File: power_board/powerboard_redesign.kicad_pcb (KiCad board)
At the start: 2 copper layers, 80 x 53 mm, 17 parts, among them J1 282834-2, J2 282834-2, J3 282834-2, J4 282834-2, U1 PDQ30-Q24-D12-D

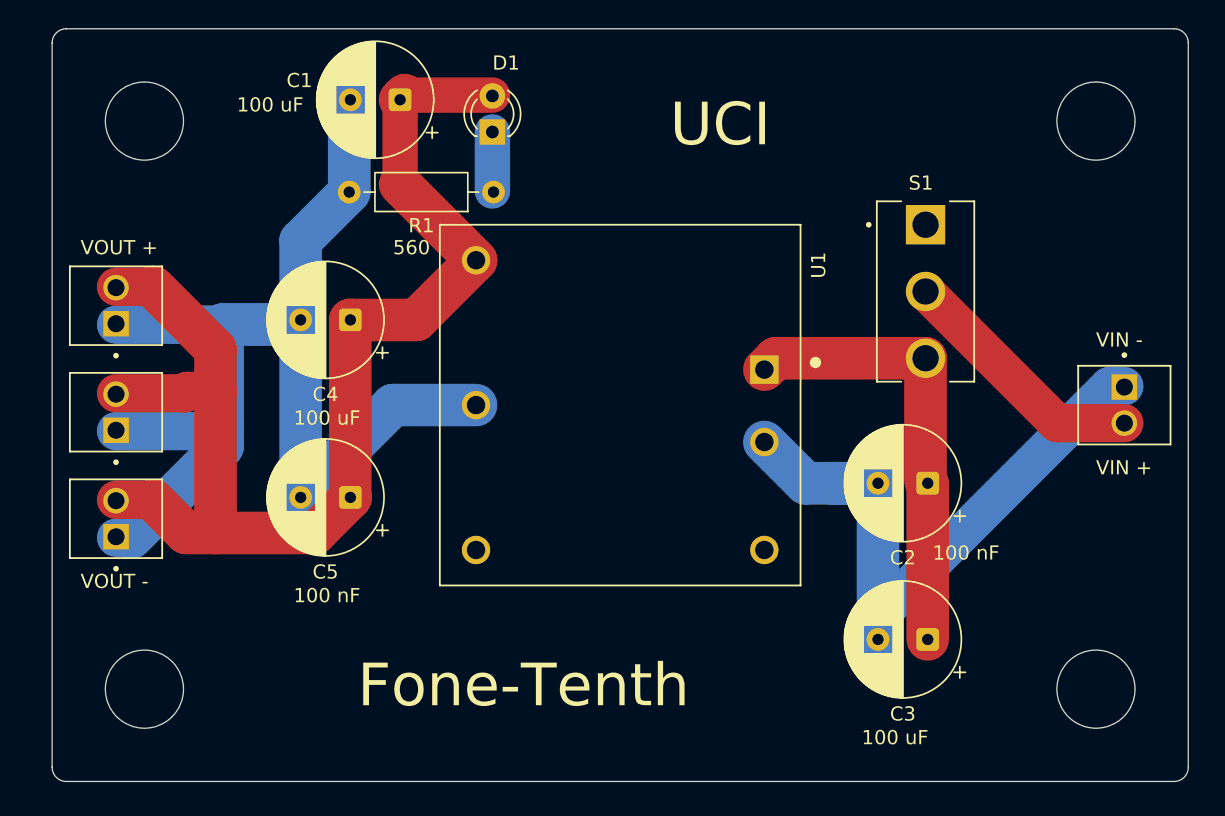
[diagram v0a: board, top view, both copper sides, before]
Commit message: Updated PCB with new connectors
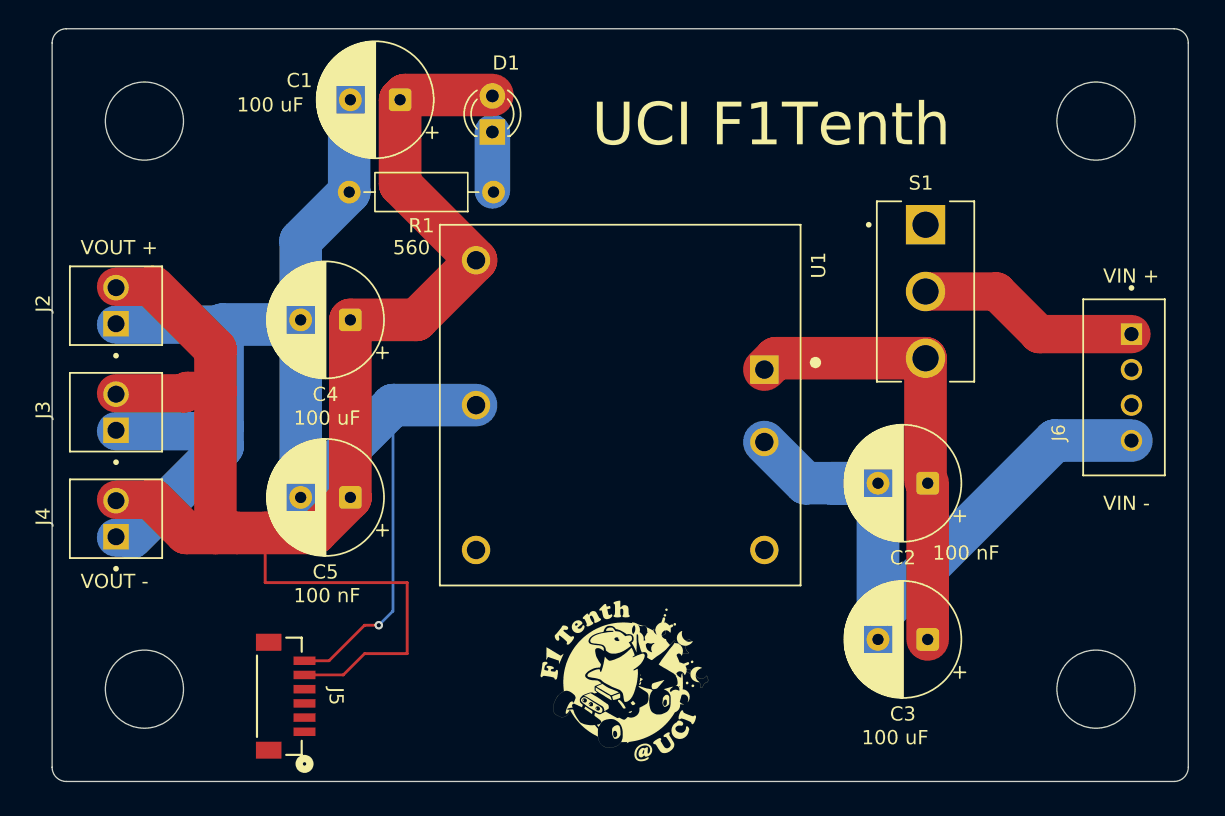
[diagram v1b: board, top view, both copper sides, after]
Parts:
- removed J1: 282834-2, Library3:TE_282834-2
- added J5: BM06B-SRSS-TBLFSN, F1TenthPowerBoard:CONN_BM06B-SRSS-TB_JST, F.Cu at (121.0, 120.0)
- added J6: B4B-XH-A, F1TenthPowerBoard:JST_B4B-XH-A, F.Cu at (180.5, 98.2)
- added Ref: LOGO, F1TenthPowerBoard:F1TenthUCILogo, F.Cu at (146.0, 119.0)
- J2, J3, J4: footprint Library3:TE_282834-2 -> F1TenthPowerBoard:TE_282834-2
- S1: footprint Library2:SW_100SP1T1B4M2QE -> F1TenthPowerBoard:SW_100SP1T1B4M2QE
- U1: footprint Library:CONV_PDQ30-Q24-D12-D -> F1TenthPowerBoard:CONV_PDQ30-Q24-D12-D
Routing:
- net Net-(D1-A): track 90.6 -> 116.9 mm
- net Net-(U1-COMMON): track 84.2 -> 106.4 mm, vias 0 -> 1
- net Net-(J6-Pad1): track 17.8 -> 15.7 mm
- net Net-(U1--VIN): track 49.2 -> 48.1 mm
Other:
- board text added: "For more information, visit: https://github.com/uci-f1tenth/Power-board Last Updated: Apr 1, 2026"
- board text added: "UCI F1Tenth"
- board text removed: "Fone-Tenth"
- board text removed: "For more information, visit: https://github.com/uci-f1tenth/Power-board Last Updated: Feb 12, 2026"
- board text removed: "UCI"

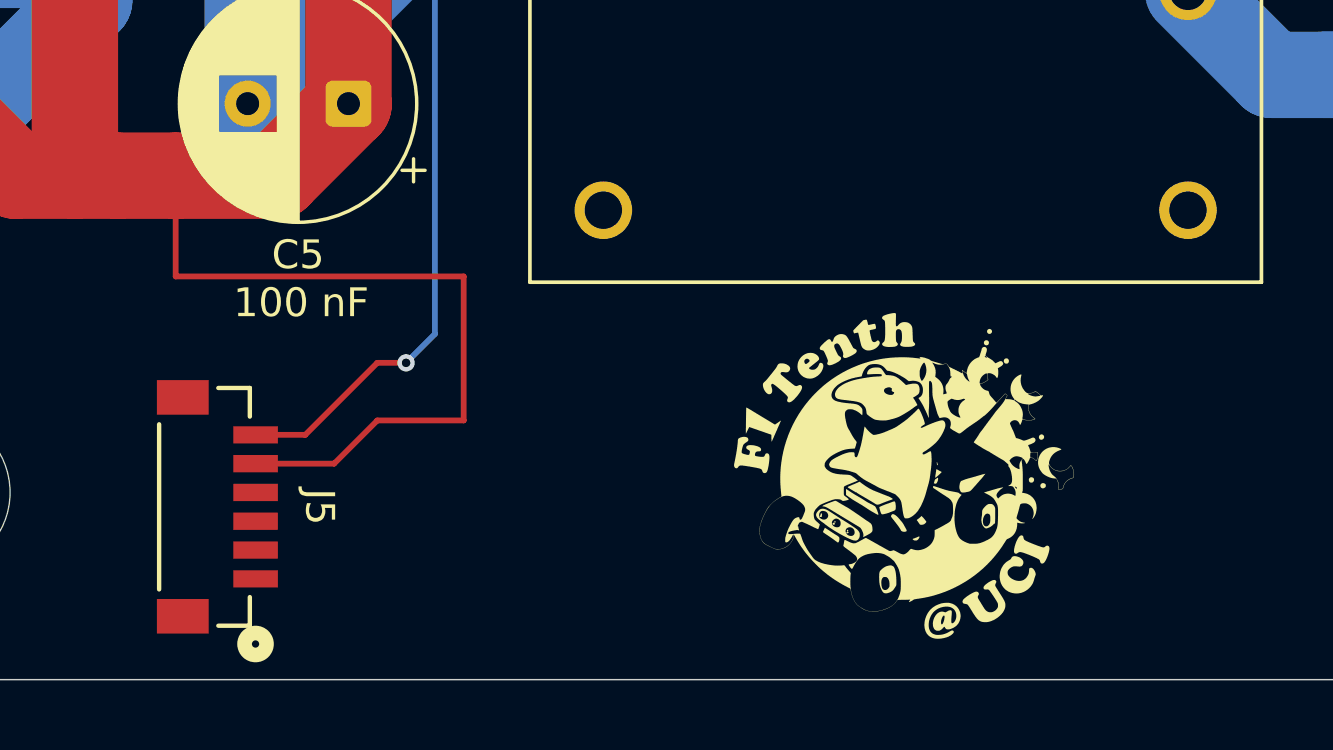
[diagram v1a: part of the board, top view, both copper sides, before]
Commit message: Updated schematic and PCB for V3
Added 4-pin connector for LiDAR connector
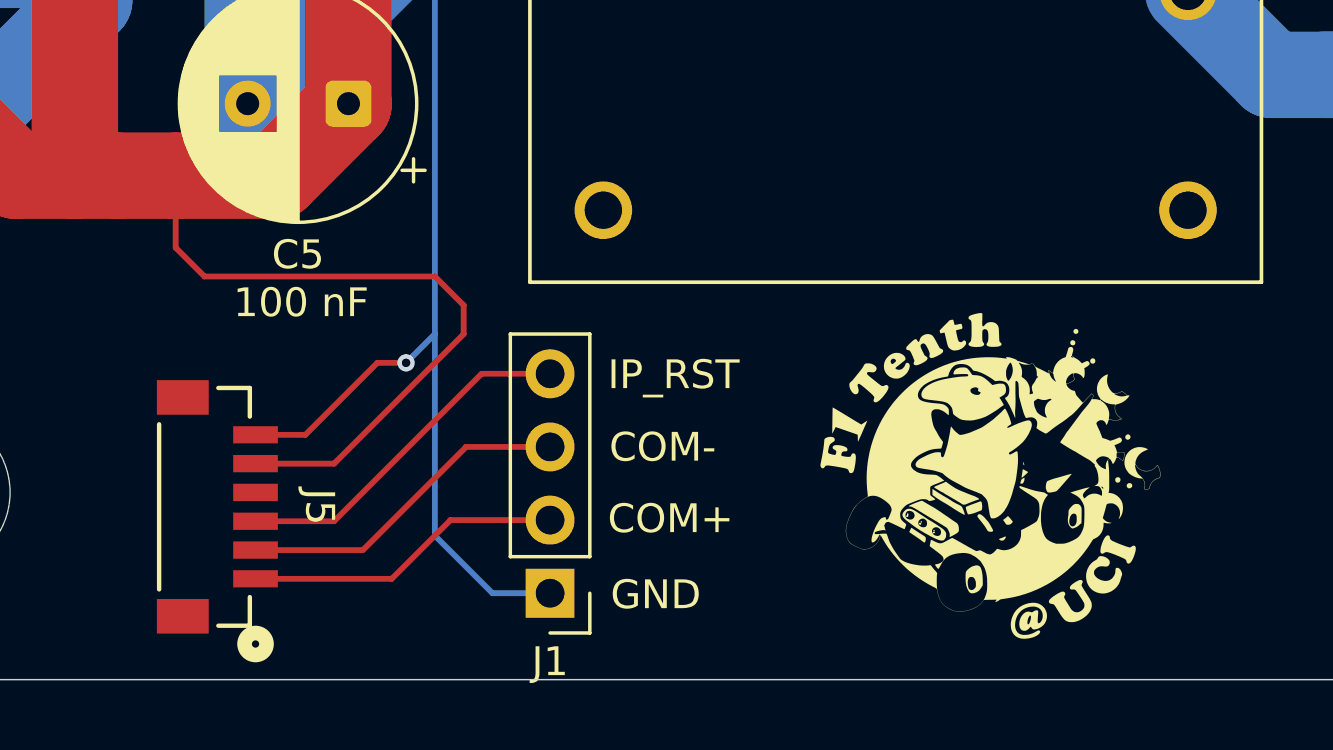
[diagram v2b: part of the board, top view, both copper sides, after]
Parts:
- added J1: Conn_01x04_Pin, Connector_PinHeader_2.54mm:PinHeader_1x04_P2.54mm_Vertical, F.Cu at (133.0, 123.0)
- moved Ref 3.00 mm to (149.0, 119.0)
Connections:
- J5 pad 1: unconnected-(J5-Pad1) -> Net-(J1-Pin_2)
- J5 pad 2: unconnected-(J5-Pad2) -> Net-(J1-Pin_3)
- J5 pad 3: unconnected-(J5-Pad3) -> Net-(J1-Pin_4)
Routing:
- net Net-(J1-Pin_4): track 0.00 -> 12.3 mm
- net Net-(J1-Pin_1): track 106.4 -> 118.2 mm
- net Net-(J1-Pin_3): track 0.00 -> 11.7 mm
- net Net-(J1-Pin_2): track 0.00 -> 11.1 mm
- net Net-(D1-A): track 116.9 -> 114.0 mm
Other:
- board text added: "COM+"
- board text added: "COM-"
- board text added: "GND"
- board text added: "IP_RST"

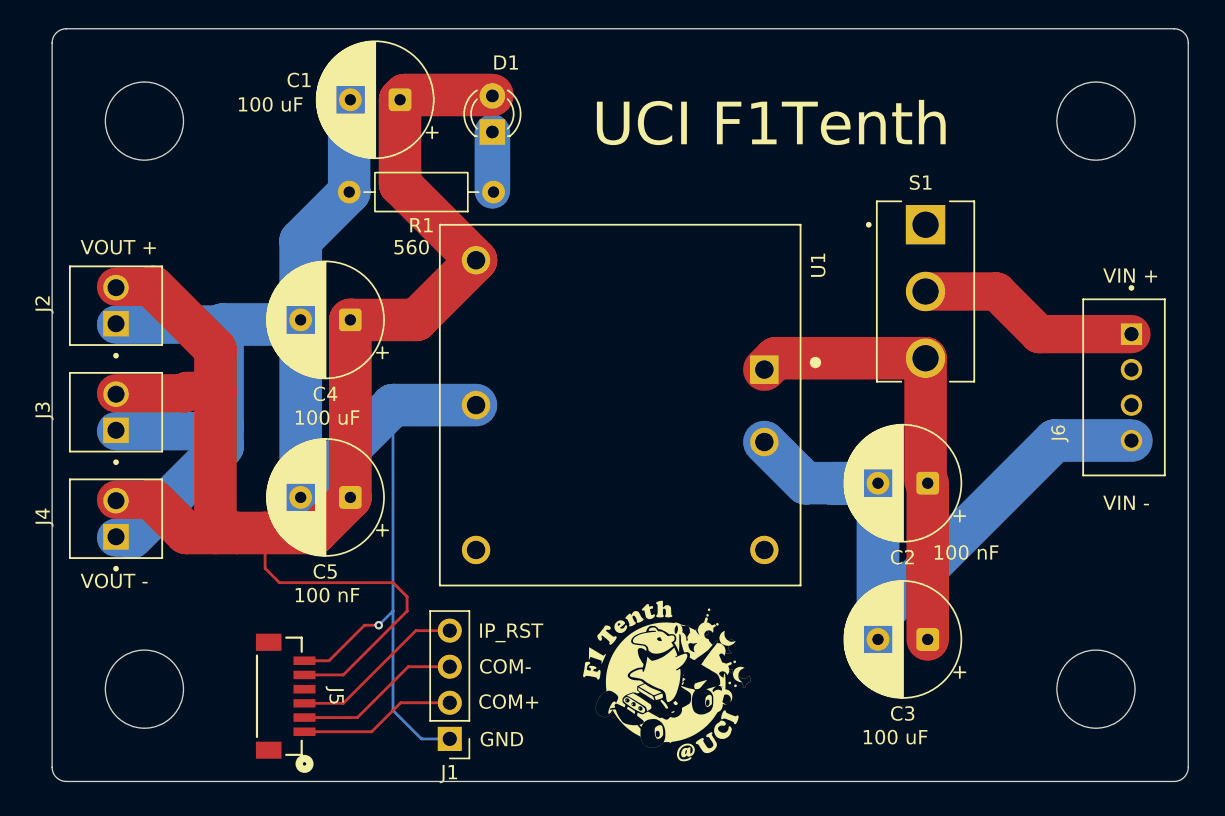
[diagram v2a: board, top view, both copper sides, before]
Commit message: Updated PCB with S12 Buck Converter + extra screw terminal block on Battery side
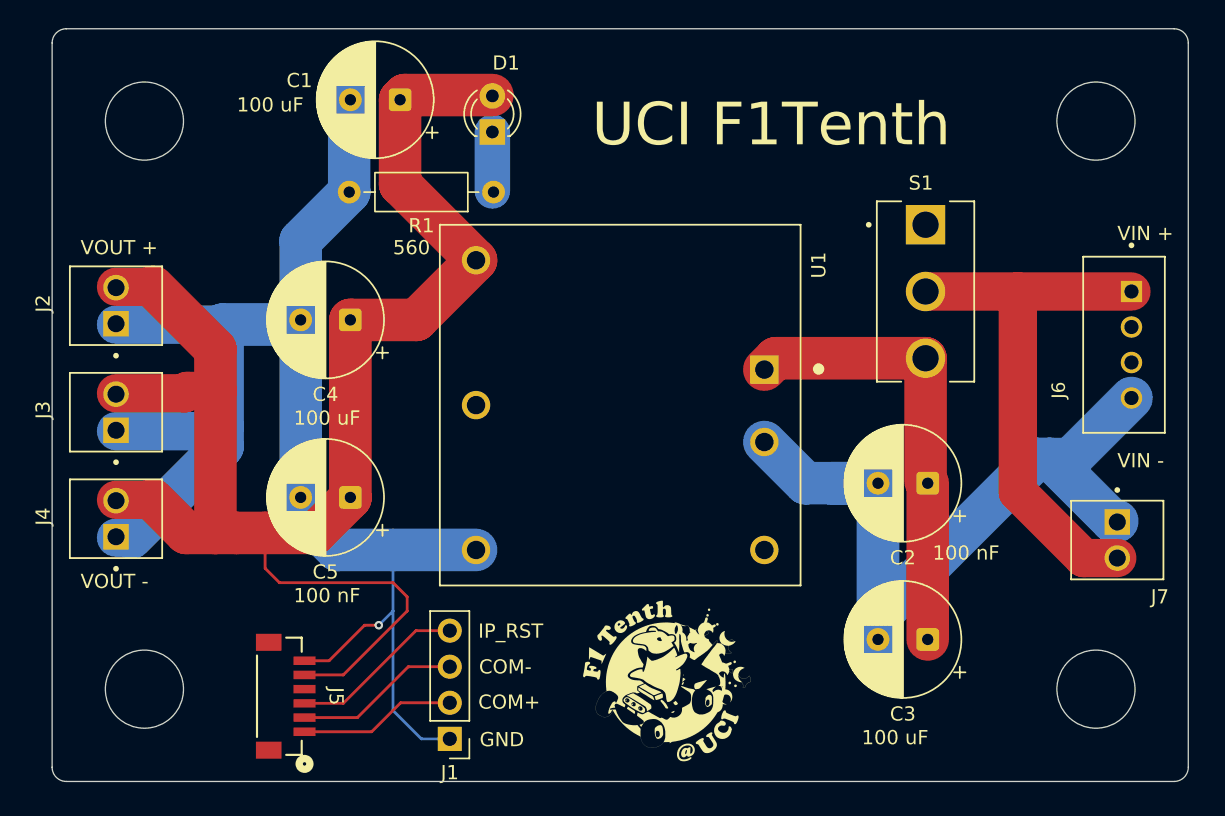
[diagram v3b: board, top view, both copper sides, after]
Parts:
- added J7: 282834-2, F1TenthPowerBoard:TE_282834-2, F.Cu at (180.0, 109.0)
- U1: value PDQ30-Q24-D12-D -> PDQ30-Q24-S12-D; footprint F1TenthPowerBoard:CONV_PDQ30-Q24-D12-D -> F1TenthPowerBoard:CONV_PDQ30-Q24-S12-D
- moved J6 3.00 mm to (180.5, 95.2)
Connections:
- U1 pad 4: Net-(J1-Pin_1) -> unconnected-(U1-TRIM-Pad4)
- U1 pad 5: unconnected-(U1--VOUT-Pad5) -> Net-(J1-Pin_1)
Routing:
- net Net-(J6-Pad1): track 15.7 -> 37.6 mm
- net Net-(J1-Pin_1): track 118.2 -> 107.7 mm
- net Net-(U1--VIN): track 48.1 -> 56.8 mm

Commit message: Updated 28 awg block with 3D model
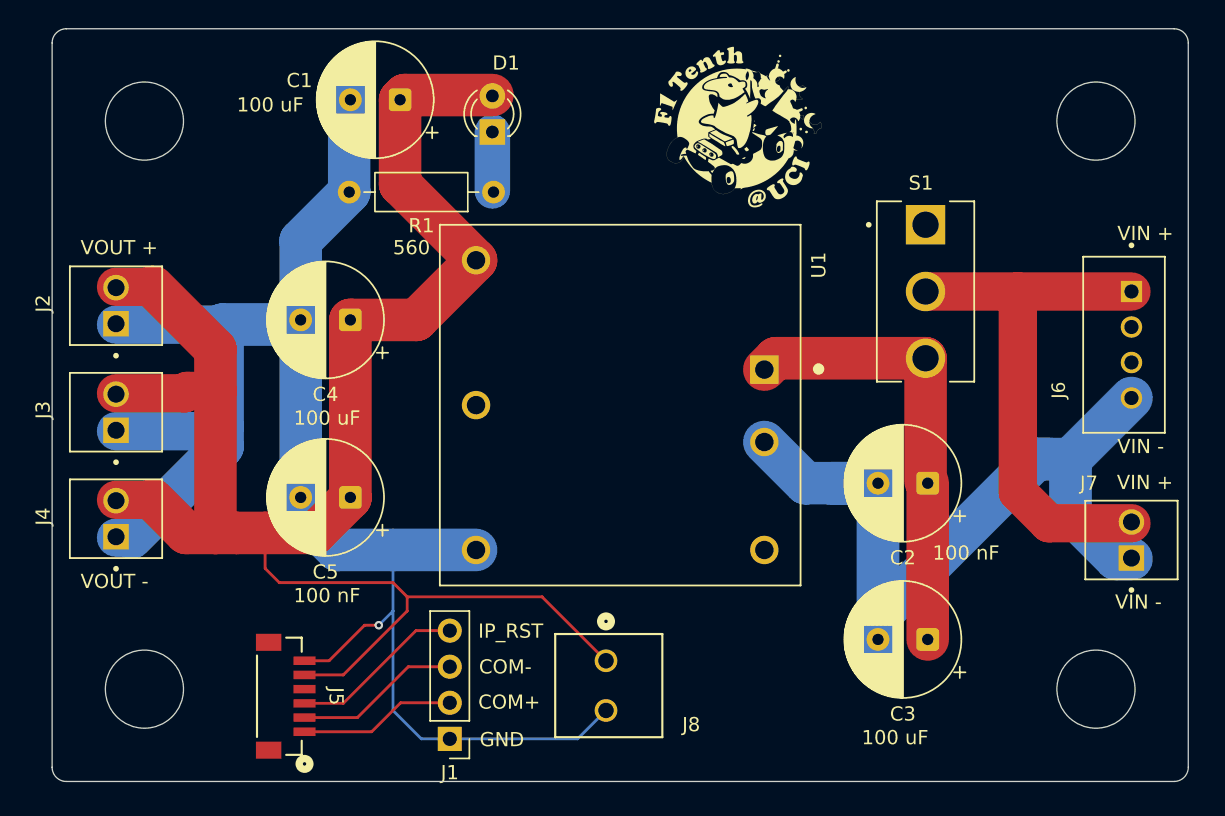
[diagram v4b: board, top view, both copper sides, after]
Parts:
- added J8: 393570002, F1TenthPowerBoard:CONN_SD-39357-001_02P_MOL, F.Cu at (144.0, 117.5)
- moved Ref 39.3 mm to (154.0, 80.0)
- moved J7 1.00 mm to (181.0, 109.0), turned to 90 degrees
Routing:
- net Net-(D1-A): track 114.0 -> 129.9 mm
- net Net-(J1-Pin_1): track 107.7 -> 119.5 mm
- net Net-(U1--VIN): track 56.8 -> 59.8 mm
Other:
- board text added: "https://github.com/uci-f1tenth/Power-board Last Updated: Apr 23, 2026"
- board text removed: "For more information, visit: https://github.com/uci-f1tenth/Power-board Last Updated: Apr 1, 2026"
- board text removed: "UCI F1Tenth"
